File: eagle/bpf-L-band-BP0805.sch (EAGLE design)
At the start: 3 parts, among them U1 BP0805, X1 SMA-142-0701-801/806, X2 SMA-142-0701-801/806

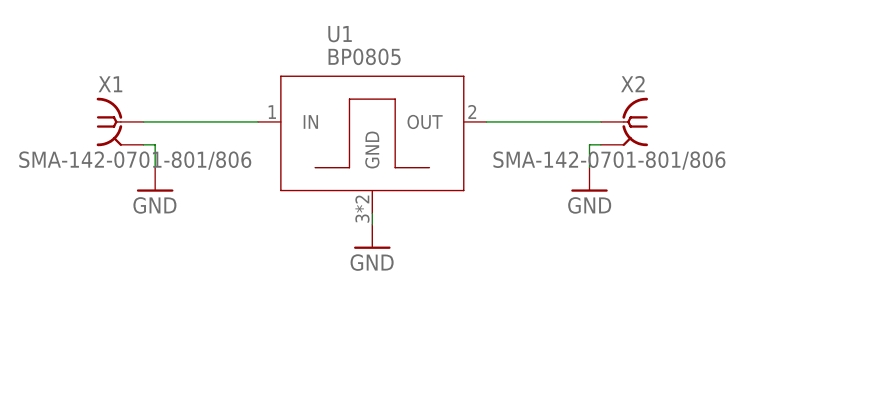
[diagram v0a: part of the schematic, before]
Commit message: Add layout for AVX BP0805
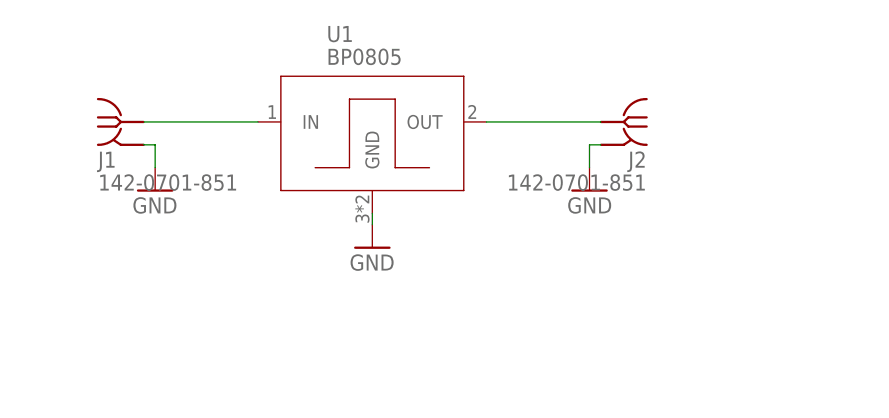
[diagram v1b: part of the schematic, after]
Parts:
- removed X1, X2: SMA-142-0701-801/806, con-coax:SMA-142-0701-801/806
- added J1, J2: 142-0701-851, J-Cinch-142-0701-851-SMA-end-launch:142-0701-851
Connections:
- removed net N$1: U1.OUT, X2.1
- removed net N$86: U1.IN, X1.1
- new net RF-IN: J1.RF, U1.IN
- new net RF-OUT: J2.RF, U1.OUT
- net GND: now also J1.GND, J2.GND; no longer X1.2, X2.2
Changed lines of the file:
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@@
 <class number="0" name="default" width="0" drill="0">
+</class>
+<class number="1" name="RF" width="0" drill="0">
+<clearance class="1" value="0.7"/>
 </class>
 </classes>
 <parts>
 <part name="FRAME2" library="frames" library_urn="urn:adsk.eagle:library:229" deviceset="FRAME_A_L" device=""/>
-<part name="X1" library="con-coax" library_urn="urn:adsk.eagle:library:133" deviceset="SMA-" device="142-0701-801/806" package3d_urn="urn:adsk.eagle:package:6214/1"/>
 <part name="GND79" library="supply1" library_urn="urn:adsk.eagle:library:371" deviceset="GND" device=""/>
-<part name="X2" library="con-coax" library_urn="urn:adsk.eagle:library:133" deviceset="SMA-" device="142-0701-801/806" package3d_urn="urn:adsk.eagle:package:6214/1"/>
 <part name="GND1" library="supply1" library_urn="urn:adsk.eagle:library:371" deviceset="GND" device=""/>
 <part name="GND2" library="supply1" library_urn="urn:adsk.eagle:library:371" deviceset="GND" device=""/>
 <part name="U1" library="U-AVX-BP0805-BPF" deviceset="BP0805" device=""/>
+<part name="J1" library="J-Cinch-142-0701-851-SMA-end-launch" deviceset="142-0701-851" device=""/>
+<part name="J2" library="J-Cinch-142-0701-851-SMA-end-launch" deviceset="142-0701-851" device=""/>
 </parts>
 <sheets>
@@
 <attribute name="DRAWING_NAME" x="190.5" y="19.05" size="2.54" layer="94"/>
 </instance>
-<instance part="X1" gate="G1" x="96.52" y="121.92" smashed="yes">
-<attribute name="VALUE" x="85.09" y="116.84" size="1.778" layer="96"/>
-<attribute name="NAME" x="93.98" y="125.222" size="1.778" layer="95"/>
-</instance>
 <instance part="GND79" gate="1" x="100.33" y="114.3" smashed="yes">
 <attribute name="VALUE" x="97.79" y="111.76" size="1.778" layer="96"/>
-</instance>
-<instance part="X2" gate="G1" x="152.4" y="121.92" smashed="yes" rot="MR0">
-<attribute name="VALUE" x="163.83" y="116.84" size="1.778" layer="96" rot="MR0"/>
-<attribute name="NAME" x="154.94" y="125.222" size="1.778" layer="95" rot="MR0"/>
 </instance>
 <instance part="GND1" gate="1" x="148.59" y="114.3" smashed="yes" rot="MR0">
@@
 <attribute name="VALUE" x="119.38" y="128.27" size="1.778" layer="96"/>
 </instance>
+<instance part="J1" gate="G$1" x="96.52" y="121.92" smashed="yes">
+<attribute name="NAME" x="93.98" y="116.84" size="1.778" layer="95"/>
+<attribute name="VALUE" x="93.98" y="114.3" size="1.778" layer="96"/>
+</instance>
+<instance part="J2" gate="G$1" x="152.4" y="121.92" smashed="yes" rot="MR0">
+<attribute name="NAME" x="154.94" y="116.84" size="1.778" layer="95" rot="MR0"/>
+<attribute name="VALUE" x="154.94" y="114.3" size="1.778" layer="96" rot="MR0"/>
+</instance>
 </instances>
 <busses>
@@
 <net name="GND" class="0">
 <segment>
-<pinref part="X1" gate="G1" pin="2"/>
 <pinref part="GND79" gate="1" pin="GND"/>
 <wire x1="99.06" y1="119.38" x2="100.33" y2="119.38" width="0.1524" layer="91"/>
 <wire x1="100.33" y1="119.38" x2="100.33" y2="116.84" width="0.1524" layer="91"/>
+<pinref part="J1" gate="G$1" pin="GND"/>
 </segment>
 <segment>
-<pinref part="X2" gate="G1" pin="2"/>
 <pinref part="GND1" gate="1" pin="GND"/>
 <wire x1="149.86" y1="119.38" x2="148.59" y2="119.38" width="0.1524" layer="91"/>
 <wire x1="148.59" y1="119.38" x2="148.59" y2="116.84" width="0.1524" layer="91"/>
+<pinref part="J2" gate="G$1" pin="GND"/>
 </segment>
 <segment>
@@
 </segment>
 </net>
-<net name="N$86" class="0">
+<net name="RF-IN" class="1">
 <segment>
-<pinref part="X1" gate="G1" pin="1"/>
 <wire x1="99.06" y1="121.92" x2="111.76" y2="121.92" width="0.1524" layer="91"/>
 <pinref part="U1" gate="G$1" pin="IN"/>
+<pinref part="J1" gate="G$1" pin="RF"/>
 </segment>
 </net>
-<net name="N$1" class="0">
+<net name="RF-OUT" class="1">
 <segment>
-<pinref part="X2" gate="G1" pin="1"/>
 <wire x1="149.86" y1="121.92" x2="137.16" y2="121.92" width="0.1524" layer="91"/>
 <pinref part="U1" gate="G$1" pin="OUT"/>
+<pinref part="J2" gate="G$1" pin="RF"/>
 </segment>
 </net>
@@
 will not be understood (or retained) with this version.
 </note>
-<note version="8.3" severity="warning">
-Since Version 8.3, EAGLE supports the association of 3D packages
-with devices in libraries, schematics, and board files. Those 3D
-packages will not be understood (or retained) with this version.
-</note>
 </compatibility>
